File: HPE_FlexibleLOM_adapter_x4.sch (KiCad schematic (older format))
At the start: 5 parts, among them J1 Connector_PCIe_x8, J2 HPE_FlexibleLOM_x8

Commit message: Do layout
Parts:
- added JP3, JP?: Jumper_3_Bridged12, Jumper:SolderJumper-3_P1.3mm_Bridged12_Pad1.0x1.5mm, symbol Jumper:Jumper_3_Bridged12
- added R2: 100kR, Resistor_SMD:R_0402_1005Metric, symbol Device:R
- R1: value 10kR -> 100kR
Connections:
- net +3V3: now also R1.2, R2.2; no longer R1.1
- net ~PERST: now also JP3.2 (C); no longer J2.A1 (~PERST)
- net at J1.A1 (~PRSNT1): now also JP?.2 (C)
- net GND: now reaches J1.A12 (GND)
- net GND: now also J1.A15 (GND), J1.A18 (GND), J1.A20 (GND), J1.A23 (GND), J1.A24 (GND), J1.A27 (GND), J1.A28 (GND), J1.A31 (GND), J1.A34 (GND), J1.A37 (GND), J1.A38 (GND), J1.A4 (GND), J1.A41 (GND), J1.A42 (GND), J1.A45 (GND), J1.A46 (GND), J1.A49 (GND), J1.B13 (GND), J1.B16 (GND), J1.B18 (GND), J1.B21 (GND), J1.B22 (GND), J1.B25 (GND), J1.B26 (GND), J1.B29 (GND), J1.B32 (GND), J1.B35 (GND), J1.B36 (GND), J1.B39 (GND), J1.B4 (GND), J1.B40 (GND), J1.B43 (GND), J1.B44 (GND), J1.B47 (GND), J1.B49 (GND), J1.B7 (GND), J2.A13 (GND), J2.A15 (GND), J2.A18 (GND), J2.A21 (GND), J2.A22 (GND), J2.A25 (GND), J2.A26 (GND), J2.A29 (GND), J2.A30 (GND), J2.A33 (GND), J2.A34 (GND), J2.A37 (GND), J2.A38 (GND), J2.A41 (GND), J2.A42 (GND), J2.A45 (GND), J2.A46 (GND), J2.A49 (GND), J2.A5 (GND), J2.A8 (GND), J2.B13 (GND), J2.B16 (GND), J2.B19 (GND), J2.B20 (GND), J2.B23 (GND), J2.B24 (GND), J2.B27 (GND), J2.B28 (GND), J2.B31 (GND), J2.B32 (GND), J2.B35 (GND), J2.B36 (GND), J2.B39 (GND), J2.B40 (GND), J2.B43 (GND), J2.B44 (GND), J2.B47 (GND), J2.B48 (GND)
- net PRSNT_x4: now reaches J1.B31 (~PRSNT2)
- net PRSNT_x4: now also JP?.3 (B)
- net PRSNT_x8: now reaches J1.B48 (~PRSNT2)
- net PRSNT_x8: now also JP?.1 (A)
- net at J2.A14 (~TRST): now also JP3.3 (B), R2.1; no longer R1.2
- new net: J2.A1 (~PERST), JP3.1 (A), R1.1
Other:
- moved on the sheet: R1

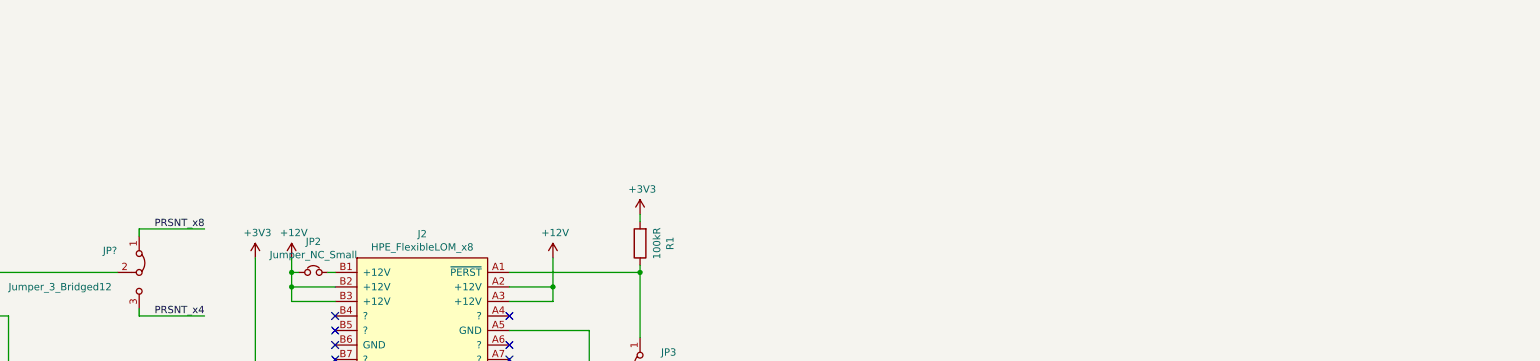
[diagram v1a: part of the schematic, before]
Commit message: Add OSHW markings
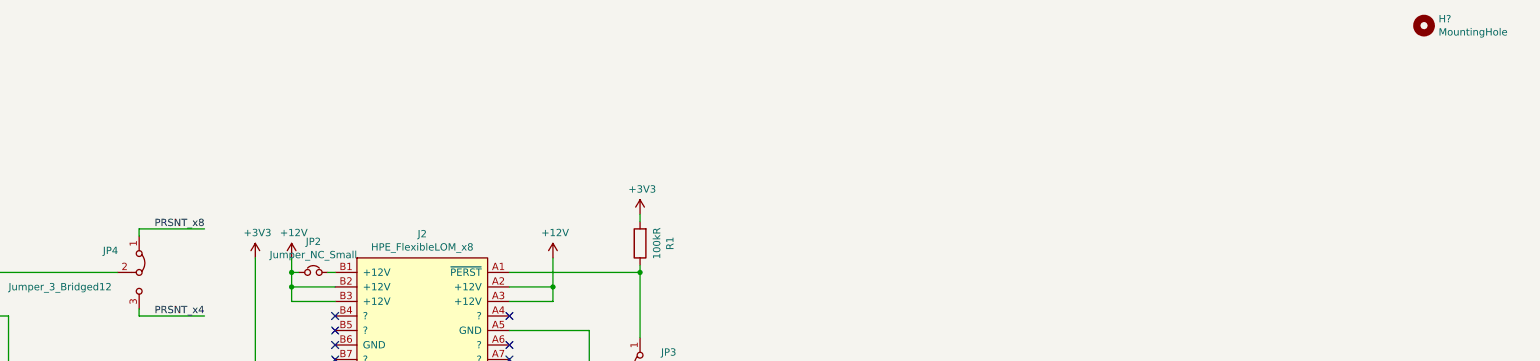
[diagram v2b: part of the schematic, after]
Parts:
- added H?: MountingHole, Symbol:OSHW-Logo2_7.3x6mm_SilkScreen, symbol Mechanical:MountingHole
- gave numbers to parts that had none: 1
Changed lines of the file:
@@
 	9750 3600 10000 3600
 $Comp
-L Jumper:Jumper_3_Bridged12 JP?
+L Jumper:Jumper_3_Bridged12 JP4
 U 1 1 5FAF2248
 P 6550 2300
-F 0 "JP?" V 6400 2050 50  0000 L CNN
+F 0 "JP4" V 6400 2050 50  0000 L CNN
 F 1 "Jumper_3_Bridged12" V 6650 1400 50  0000 L CNN
 F 2 "Jumper:SolderJumper-3_P1.3mm_Bridged12_Pad1.0x1.5mm" H 6550 2300 50  0001 C CNN
@@
 Wire Wire Line
 	3500 5300 3900 5300
+$Comp
+L Mechanical:MountingHole H?
+U 1 1 5FBB5975
+P 15400 600
+F 0 "H?" H 15500 646 50  0000 L CNN
+F 1 "MountingHole" H 15500 555 50  0000 L CNN
+F 2 "Symbol:OSHW-Logo2_7.3x6mm_SilkScreen" H 15400 600 50  0001 C CNN
+F 3 "~" H 15400 600 50  0001 C CNN
+	1    15400 600
+	1    0    0    -1
+$EndComp
 $EndSCHEMATC

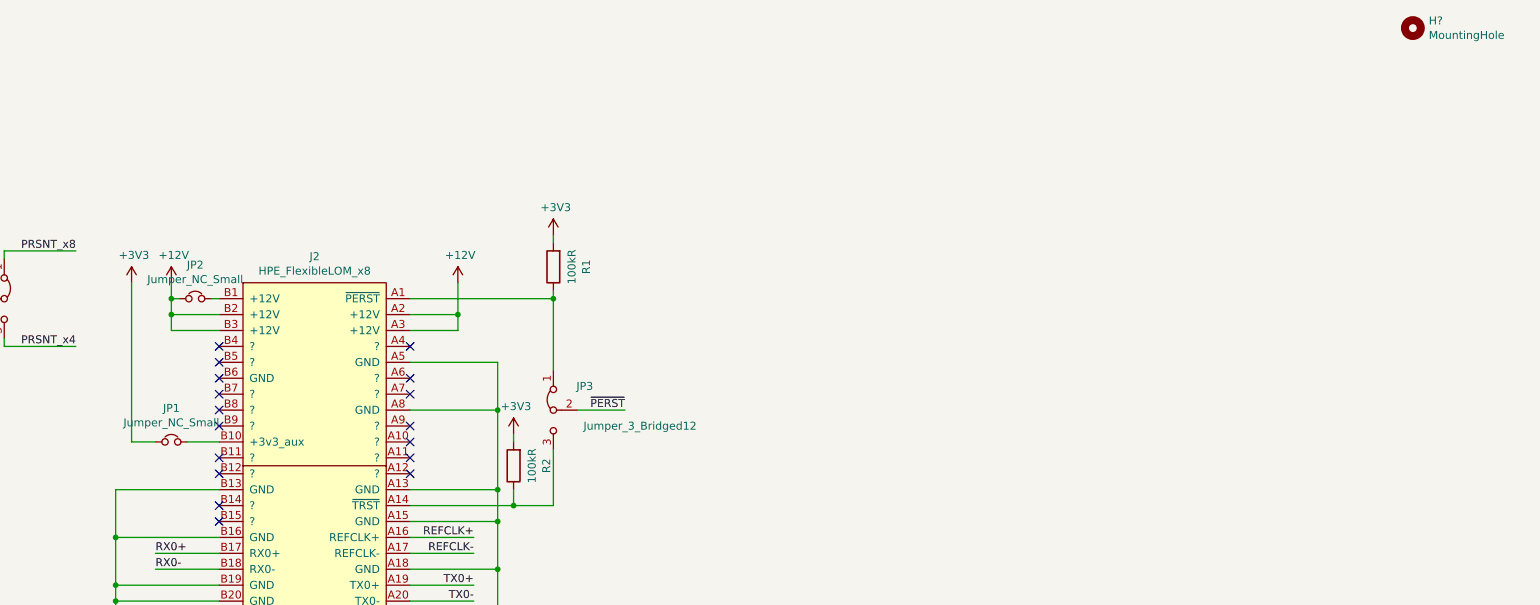
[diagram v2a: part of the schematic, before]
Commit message: Reverse engineer some more FlexibleLOM signals
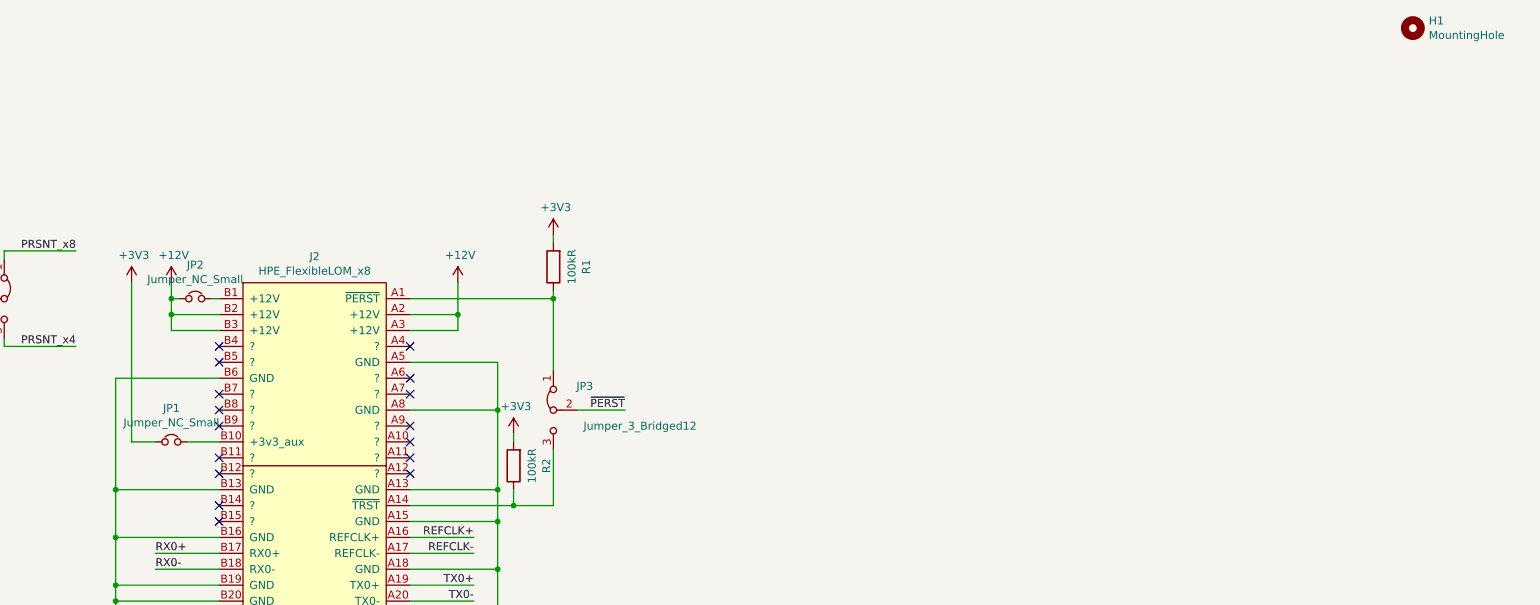
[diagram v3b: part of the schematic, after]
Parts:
- H1: renamed from H?; footprint Symbol:OSHW-Logo2_7.3x6mm_SilkScreen -> Symbol:OSHW-Symbol_6.7x6mm_SilkScreen
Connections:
- net GND: now also J2.B6 (GND)
- no-connect marks 17 -> 16
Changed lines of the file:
@@
 NoConn ~ 7900 2600
 NoConn ~ 7900 2700
-NoConn ~ 7900 2800
 NoConn ~ 7900 2900
 NoConn ~ 7900 3000
@@
 	3500 5300 3900 5300
 $Comp
-L Mechanical:MountingHole H?
+L Mechanical:MountingHole H1
 U 1 1 5FBB5975
 P 15400 600
-F 0 "H?" H 15500 646 50  0000 L CNN
+F 0 "H1" H 15500 646 50  0000 L CNN
 F 1 "MountingHole" H 15500 555 50  0000 L CNN
-F 2 "Symbol:OSHW-Logo2_7.3x6mm_SilkScreen" H 15400 600 50  0001 C CNN
+F 2 "Symbol:OSHW-Symbol_6.7x6mm_SilkScreen" H 15400 600 50  0001 C CNN
 F 3 "~" H 15400 600 50  0001 C CNN
 	1    15400 600
 	1    0    0    -1
 $EndComp
+Wire Wire Line
+	7900 2800 7250 2800
+Wire Wire Line
+	7250 2800 7250 3500
+Connection ~ 7250 3500
 $EndSCHEMATC
